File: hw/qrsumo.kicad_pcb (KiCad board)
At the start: 2 copper layers, 50 x 70 mm, 0 parts

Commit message: adding first layout
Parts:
- added C1: 4.7u, Capacitor_SMD:C_0603_1608Metric, F.Cu at (130.1, 160.8)
- added C2: 4.7u, Capacitor_SMD:C_0603_1608Metric, F.Cu at (129.5, 156.8)
- added C3: 47u, Capacitor_SMD:C_0603_1608Metric, F.Cu at (132.6, 156.8)
- added C4: 10u, Capacitor_SMD:C_0603_1608Metric, F.Cu at (110.0, 127.2)
- added C5: 0.1u, Capacitor_SMD:C_0603_1608Metric, F.Cu at (111.6, 127.4)
- added C6: 2.2u, Capacitor_SMD:C_0603_1608Metric, F.Cu at (128.8, 149.6)
- added C7: 22u, Capacitor_SMD:C_0603_1608Metric, F.Cu at (128.8, 152.4)
- added C8: 10u, Capacitor_SMD:C_0603_1608Metric, F.Cu at (119.4, 121.4)
- added D1: LED_Small, Connector_PinHeader_2.54mm:PinHeader_1x02_P2.54mm_Vertical, F.Cu at (112.0, 105.3)
- added D10: GREEN, LED_SMD:LED_0603_1608Metric, F.Cu at (136.9, 148.8)
- added D11: RED, LED_SMD:LED_0603_1608Metric, F.Cu at (141.0, 148.8)
- added D12: WS2812B, LED_SMD:LED_WS2812B_PLCC4_5.0x5.0mm_P3.2mm, F.Cu at (124.1, 122.1)
- added D2: LED_Small, Connector_PinHeader_2.54mm:PinHeader_1x02_P2.54mm_Vertical, F.Cu at (126.6, 103.0)
- added D3: LED_Small, Connector_PinHeader_2.54mm:PinHeader_1x02_P2.54mm_Vertical, F.Cu at (137.8, 107.1)
- added D4: BLUE, LED_SMD:LED_0603_1608Metric, F.Cu at (138.3, 113.0)
- added D5: D_Schottky, Diode_SMD:D_SOD-123F, F.Cu at (111.4, 161.2)
- added D6: D_Photo, Connector_PinHeader_2.54mm:PinHeader_1x02_P2.54mm_Vertical, F.Cu at (108.0, 109.3)
- added D7: D_Photo, Connector_PinHeader_2.54mm:PinHeader_1x02_P2.54mm_Vertical, F.Cu at (119.3, 103.0)
- added D8: D_Photo, Connector_PinHeader_2.54mm:PinHeader_1x02_P2.54mm_Vertical, F.Cu at (133.2, 102.6)
- added D9: YELLOW, LED_SMD:LED_0603_1608Metric, F.Cu at (106.9, 140.8)
- added J1: Conn_01x02, Connector_PinHeader_2.54mm:PinHeader_1x02_P2.54mm_Vertical, F.Cu at (147.9, 156.7)
- added J2: USB_B_Micro, QRsumo_FootprintLibrary:CONN_10118193-0001LF_AMP, F.Cu at (114.4, 166.7)
- added J3: UART, Connector_PinHeader_2.54mm:PinHeader_1x03_P2.54mm_Vertical, F.Cu at (147.6, 117.0)
- added J4: MOTOR_LEFT, Connector_PinHeader_2.54mm:PinHeader_1x02_P2.54mm_Vertical, F.Cu at (102.1, 148.5)
- added J5: MOTOR_RIGHT, Connector_PinHeader_2.54mm:PinHeader_1x02_P2.54mm_Vertical, F.Cu at (147.9, 148.7)
- added J6: Conn_01x07, Connector_PinHeader_2.54mm:PinHeader_1x07_P2.54mm_Vertical, F.Cu at (102.7, 127.4)
- added J7: Conn_01x07, Connector_PinHeader_2.54mm:PinHeader_1x07_P2.54mm_Vertical, F.Cu at (147.6, 126.6)
- added J8: VBAT, Connector_PinHeader_2.54mm:PinHeader_1x02_P2.54mm_Vertical, F.Cu at (139.9, 167.8)
- added Q1: AO3400A, Package_TO_SOT_SMD:SOT-23, F.Cu at (142.6, 114.8)
- added Q2: DMG2301L, Package_TO_SOT_SMD:SOT-23, F.Cu at (142.6, 159.2)
- added Q3: DMG2301L, Package_TO_SOT_SMD:SOT-23, F.Cu at (138.5, 163.2)
- added Q4: GP2S60, QRsumo_FootprintLibrary:SHARP_GP2S60, B.Cu at (110.4, 102.1)
- added Q5: GP2S60, QRsumo_FootprintLibrary:SHARP_GP2S60, B.Cu at (141.0, 102.2)
- added Q6: AO3400A, Package_TO_SOT_SMD:SOT-23, F.Cu at (106.2, 118.4)
- added Q7: GP2S60, QRsumo_FootprintLibrary:SHARP_GP2S60, B.Cu at (122.5, 155.4)
- added R1: 33, Resistor_SMD:R_0603_1608Metric, F.Cu at (115.0, 107.1)
- added R10: 33, Resistor_SMD:R_0603_1608Metric, F.Cu at (115.8, 116.3)
- added R11: 33, Resistor_SMD:R_0603_1608Metric, F.Cu at (130.1, 115.2)
- added R12: 1k, Resistor_SMD:R_0603_1608Metric, F.Cu at (118.3, 112.4)
- added R13: 1k, Resistor_SMD:R_0603_1608Metric, F.Cu at (118.4, 117.1)
- added R14: 1k, Resistor_SMD:R_0603_1608Metric, F.Cu at (129.3, 117.6)
- added R15: 1k, Resistor_SMD:R_0603_1608Metric, F.Cu at (106.8, 143.8)
- added R16: 1k, Resistor_SMD:R_0603_1608Metric, F.Cu at (136.1, 152.3)
- added R17: 1k, Resistor_SMD:R_0603_1608Metric, F.Cu at (140.4, 152.4)
- added R18: 10k, Resistor_SMD:R_0603_1608Metric, F.Cu at (110.9, 129.7)
- added R19: 5k, Resistor_SMD:R_0603_1608Metric, F.Cu at (133.3, 162.4)
- added R2: 33, Resistor_SMD:R_0603_1608Metric, F.Cu at (128.2, 105.8)
- added R20: 10k, Resistor_SMD:R_0603_1608Metric, F.Cu at (133.3, 159.6)
- added R21: 1k, Resistor_SMD:R_0603_1608Metric, B.Cu at (114.2, 102.7)
- added R22: 1k, Resistor_SMD:R_0603_1608Metric, F.Cu at (107.0, 103.7)
- added R23: 5k, Resistor_SMD:R_0603_1608Metric, F.Cu at (110.1, 157.9)
- added R24: 10k, Resistor_SMD:R_0603_1608Metric, F.Cu at (111.4, 154.6)
- added R25: 1k, Resistor_SMD:R_0603_1608Metric, B.Cu at (144.8, 102.8)
- added R26: 1k, Resistor_SMD:R_0603_1608Metric, F.Cu at (140.9, 105.3)
- added R27: 1k, Resistor_SMD:R_0603_1608Metric, B.Cu at (124.7, 157.7)
- added R28: 1k, Resistor_SMD:R_0603_1608Metric, B.Cu at (120.3, 157.6)
- added R29: 10k, Resistor_SMD:R_0603_1608Metric, F.Cu at (136.3, 143.3)
- added R3: 33, Resistor_SMD:R_0603_1608Metric, F.Cu at (136.0, 110.3)
- added R30: 10k, Resistor_SMD:R_0603_1608Metric, F.Cu at (142.7, 117.8)
- added R31: 100, Resistor_SMD:R_0603_1608Metric, F.Cu at (140.1, 118.6)
- added R32: 10k, Resistor_SMD:R_0603_1608Metric, F.Cu at (109.1, 118.3)
- added R33: 100, Resistor_SMD:R_0603_1608Metric, F.Cu at (108.1, 121.0)
- added R4: 1k, Resistor_SMD:R_0603_1608Metric, F.Cu at (138.3, 114.7)
- added R5: 10k, Resistor_SMD:R_0603_1608Metric, F.Cu at (112.9, 157.9)
- added R6: 1k, Resistor_SMD:R_0603_1608Metric, F.Cu at (103.1, 113.6)
- added R7: 1k, Resistor_SMD:R_0603_1608Metric, F.Cu at (120.7, 105.8)
- added R8: 1k, Resistor_SMD:R_0603_1608Metric, F.Cu at (145.1, 110.9)
- added R9: 33, Resistor_SMD:R_0603_1608Metric, F.Cu at (115.9, 113.1)
- added SW1: SW_SPDT, QRsumo_FootprintLibrary:EG1206A_EWI, F.Cu at (125.0, 166.8)
- added SW2: SW_SPST, QRsumo_FootprintLibrary:PTS647_SPST_SNXX_SMTR2_4.5x4.5mm, F.Cu at (140.2, 132.4)
- added SW3: SW_SPST, QRsumo_FootprintLibrary:PTS647_SPST_SNXX_SMTR2_4.5x4.5mm, F.Cu at (140.8, 140.6)
- added U1: LMV324, Package_SO:TSSOP-14_4.4x5mm_P0.65mm, F.Cu at (123.8, 114.8)
- added U2: AP7361C-33E, Package_TO_SOT_SMD:SOT-223-3_TabPin2, F.Cu at (123.3, 158.9)
- added U3: DRV8833PWP, Package_SO:HTSSOP-16-1EP_4.4x5mm_P0.65mm_EP3.4x5mm_Mask2.46x2.31mm_ThermalVias, F.Cu at (122.2, 151.4)
- added U4: TSOP382xx, OptoDevice:Vishay_MINICAST-3Pin, F.Cu at (108.3, 132.4)
- added U5: ESP32-S3-WROOM-1, Espressif:ESP32-S3-WROOM-1U, F.Cu at (125.1, 135.5)
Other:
- outline, holes or cut-outs redrawn
- copper layers 2 -> 4

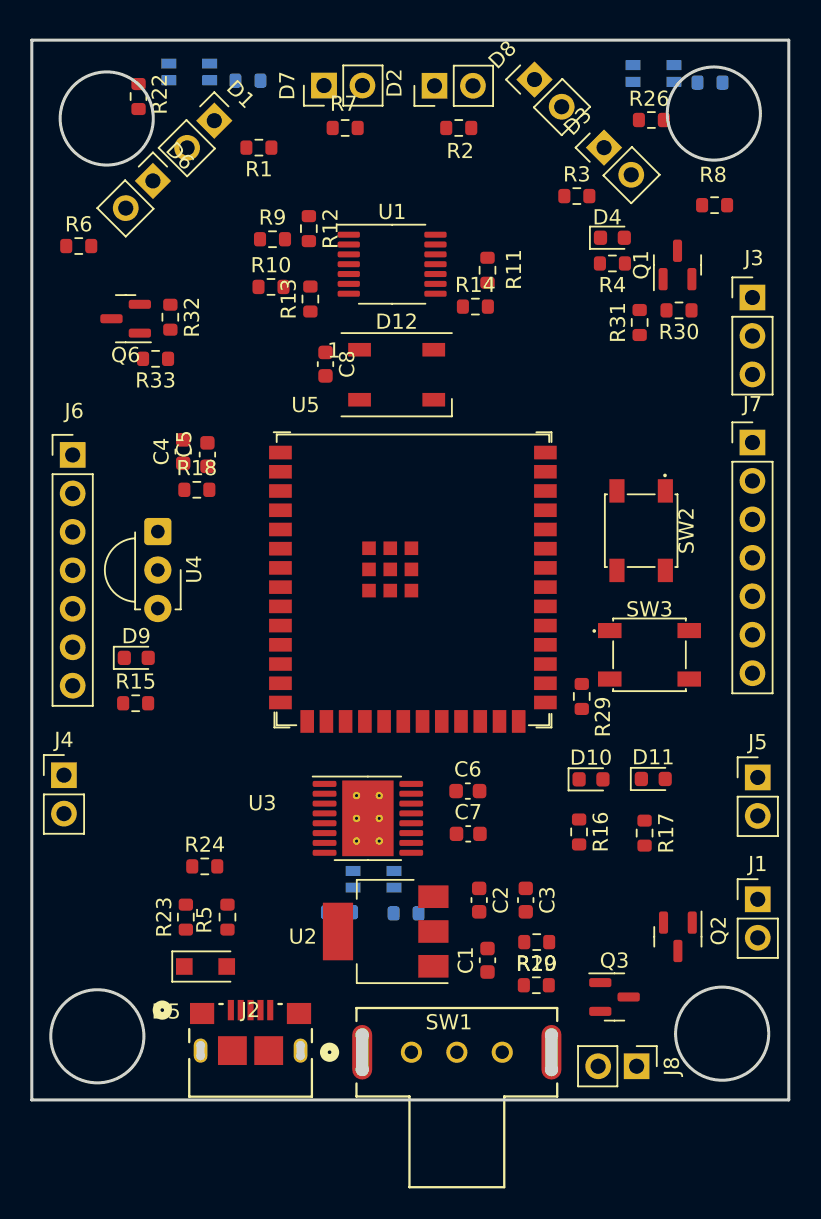
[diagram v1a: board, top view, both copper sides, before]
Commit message: Improve placement, fix footprints
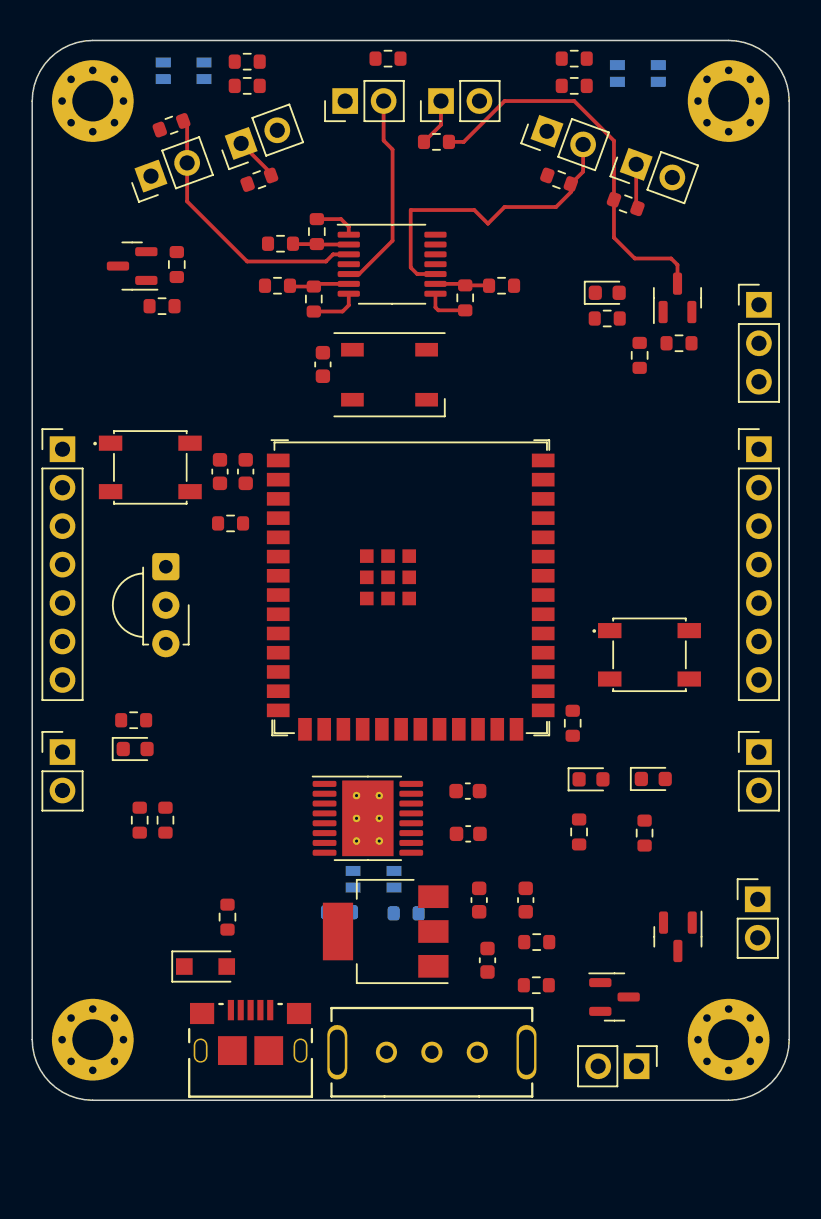
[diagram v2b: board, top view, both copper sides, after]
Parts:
- added H1: MountingHole_Pad, MountingHole:MountingHole_2.7mm_M2.5_Pad_Via, F.Cu at (104.0, 166.0)
- added H2: MountingHole_Pad, MountingHole:MountingHole_2.7mm_M2.5_Pad_Via, F.Cu at (104.0, 104.0)
- added H3: MountingHole_Pad, MountingHole:MountingHole_2.7mm_M2.5_Pad_Via, F.Cu at (146.0, 166.0)
- added H4: MountingHole_Pad, MountingHole:MountingHole_2.7mm_M2.5_Pad_Via, F.Cu at (146.0, 104.0)
- R21, R25: moved to F.Cu
- moved SW2 32.7 mm to (107.8, 128.2), turned to 0 degrees
- moved R8 10.4 mm to (134.8, 109.2), turned to -20 degrees
- moved R6 10.1 mm to (109.2, 105.6), turned to 20 degrees
- moved R25 9.11 mm to (135.8, 101.2), turned to 0 degrees
- moved R22 7.21 mm to (114.2, 103.0), turned to 0 degrees
- moved R23 7.09 mm to (107.1, 151.5)
- moved D9 6.02 mm to (106.8, 146.8)
- moved R26 5.57 mm to (135.8, 103.0)
- moved R7 5.38 mm to (123.5, 101.2)
- moved R24 4.01 mm to (108.8, 151.5), turned to -90 degrees
- moved D4 3.65 mm to (138.0, 116.7)
- moved R4 3.65 mm to (138.0, 118.4)
- moved D8 3.52 mm to (134.0, 106.0), turned to 70 degrees
- moved R33 3.50 mm to (108.6, 117.5)
- moved R32 3.50 mm to (109.5, 114.8)
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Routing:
- net Net-(Q1-Pad3): track 0.00 -> 25.7 mm
- net Net-(D8-Pad2): track 0.00 -> 20.9 mm
- net Net-(D6-Pad2): track 0.00 -> 17.9 mm
- net Net-(D7-Pad2): track 0.00 -> 13.3 mm
- net Net-(R10-Pad2): track 0.00 -> 3.98 mm
- net Net-(R12-Pad2): track 0.00 -> 3.71 mm
- net Net-(R11-Pad2): track 0.00 -> 3.59 mm
- net /RANGE_FRONT_CENTER: track 0.00 -> 3.24 mm
- net Net-(D2-Pad1): track 0.00 -> 3.17 mm
- net /RANGE_FRONT_RIGHT: track 0.00 -> 2.95 mm
- net Net-(D3-Pad1): track 0.00 -> 2.94 mm
- net Net-(D1-Pad1): track 0.00 -> 2.94 mm
- net /RANGE_FRONT_LEFT: track 0.00 -> 2.92 mm
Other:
- outline, holes or cut-outs redrawn
